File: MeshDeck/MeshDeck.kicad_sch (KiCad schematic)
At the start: 4 parts, among them CN1 ATGM336H-6N-74, U1 ESP32-S3-WROOM-1(N16R8), U2 SX1262S8S+T-X1, U3 TPS62827ADMQR

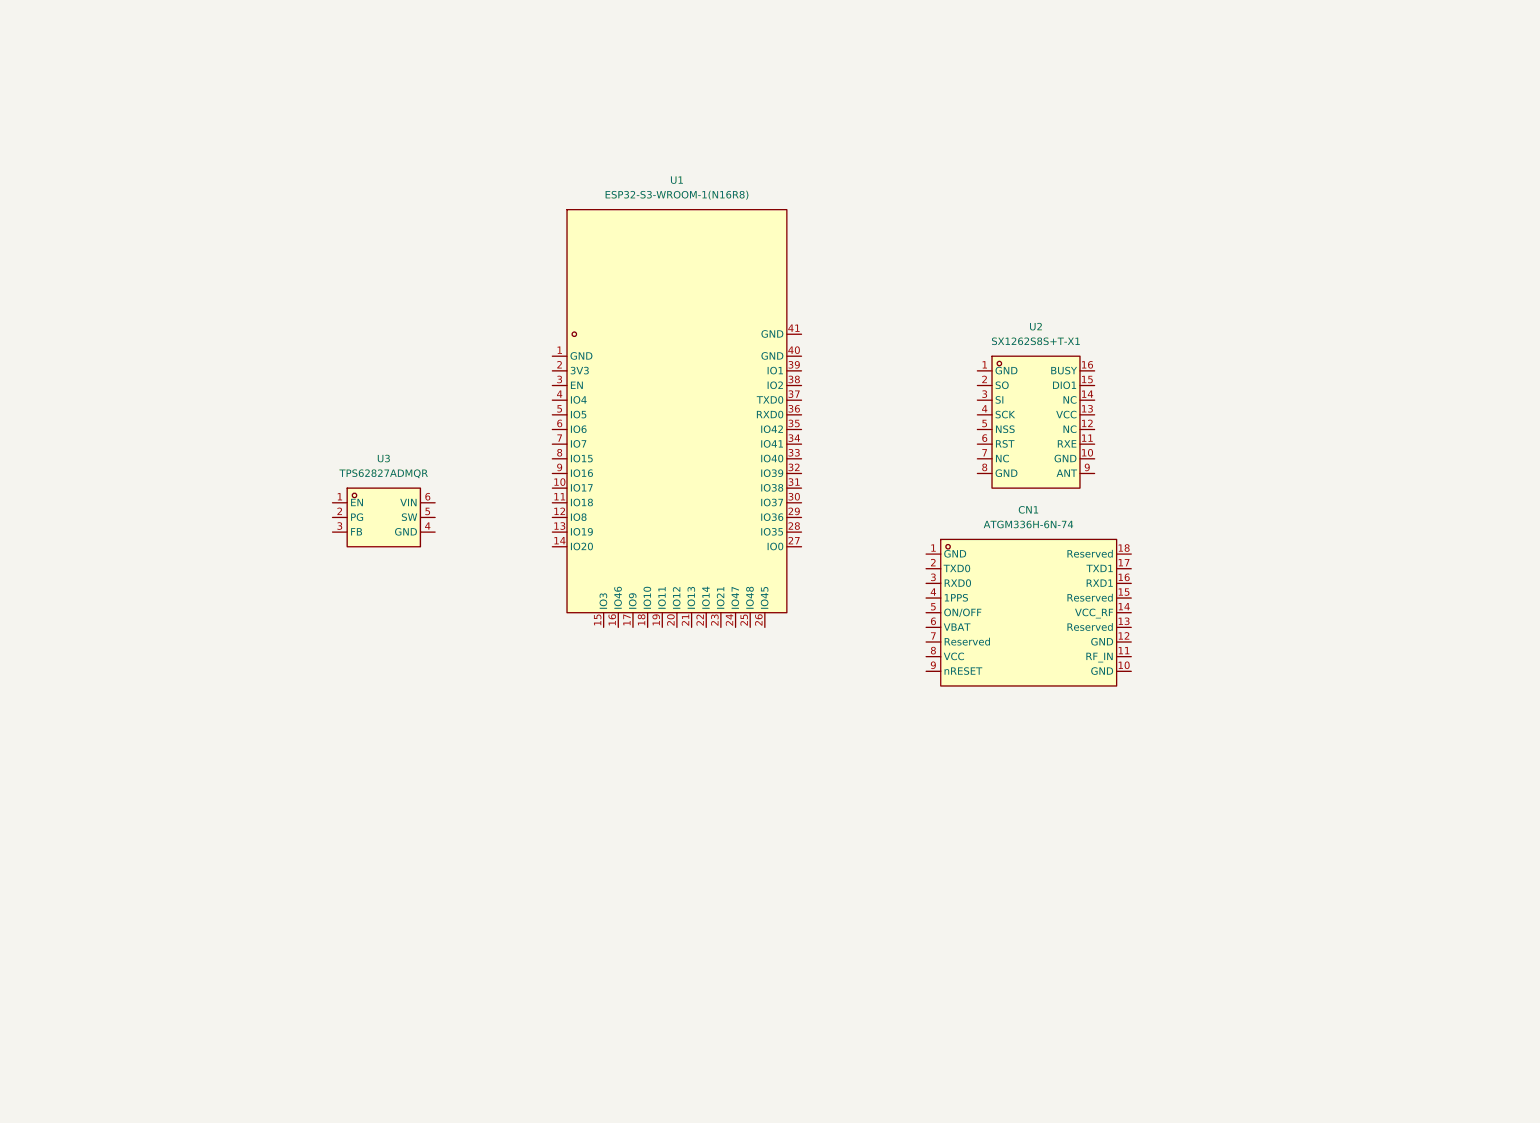
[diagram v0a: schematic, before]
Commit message: Added ESP-32 and USB stuff
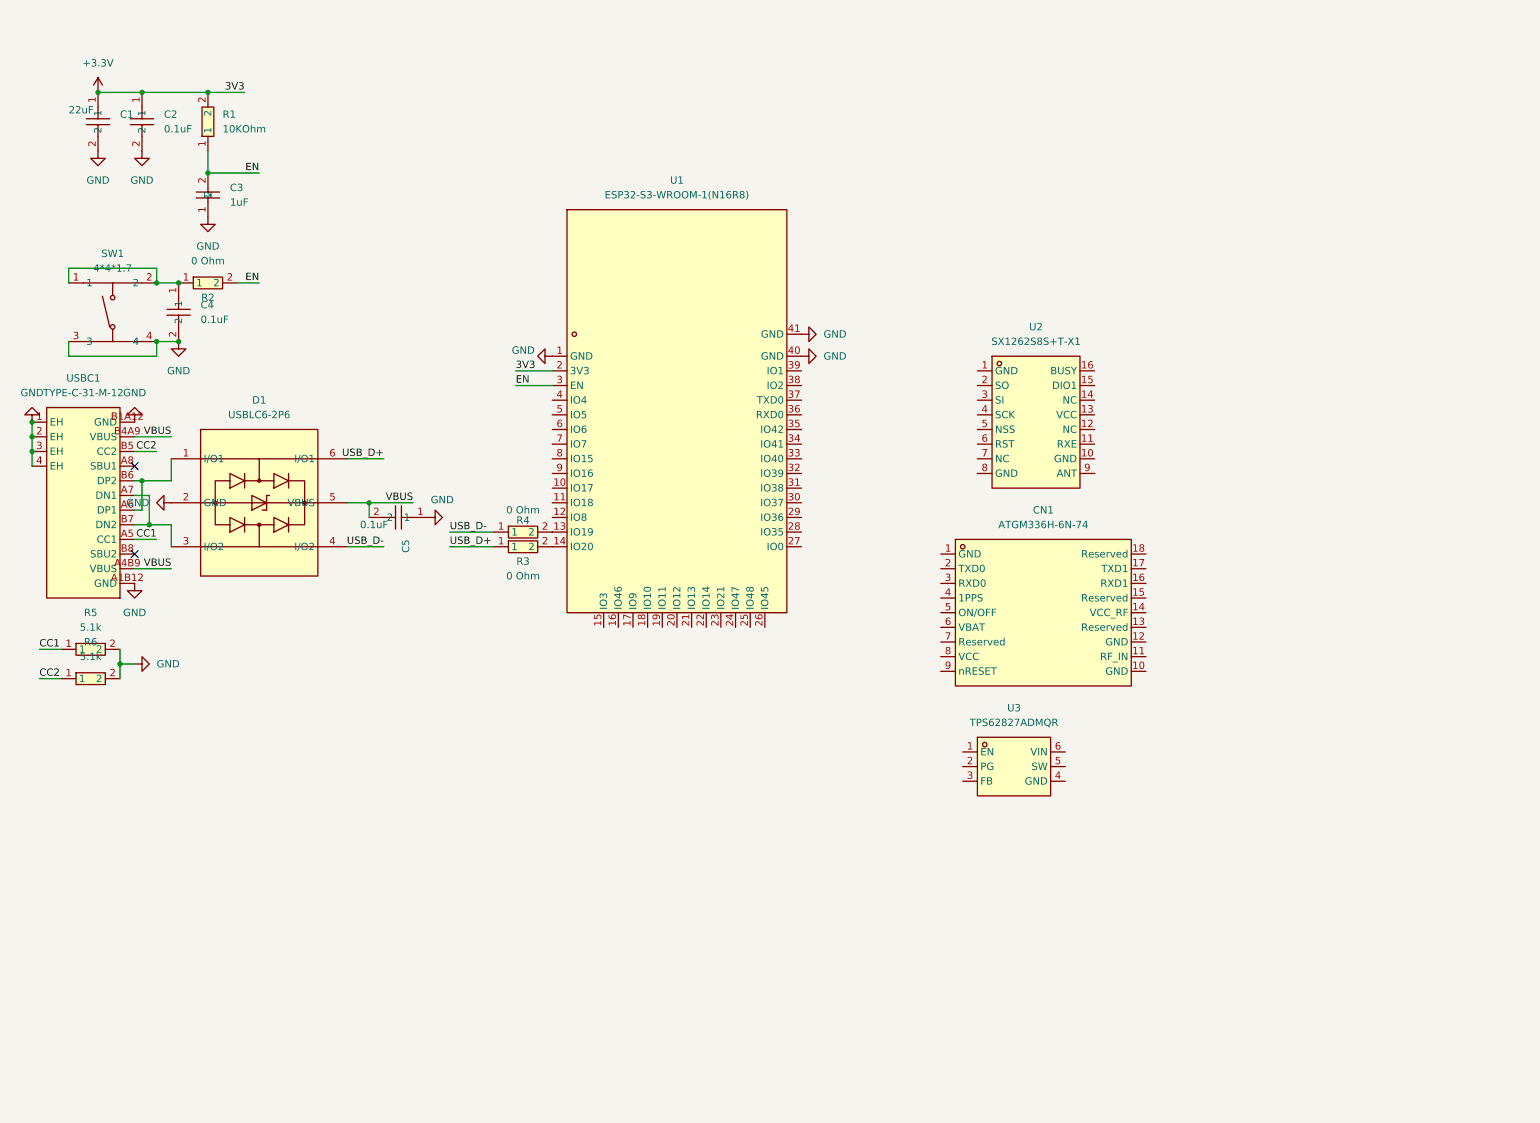
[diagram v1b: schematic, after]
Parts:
- added C1: 22uF, MeshDeck:C0402, symbol MeshDeck:CL05A226MQ5QUNC
- added C2, C4, C5: 0.1uF, MeshDeck:C0402, symbol MeshDeck:CL05B104KO5NNNC
- added C3: 1uF, MeshDeck:C0402, symbol MeshDeck:CL05A105KP5NNNC
- added D1: USBLC6-2P6, MeshDeck:SOT-666-6_L1.6-W1.2-P0.50-LS1.6-BR, symbol MeshDeck:USBLC6-2P6
- added R1: 10KOhm, MeshDeck:R0402, symbol MeshDeck:QR0402F1KQ10
- added R2, R3, R4: 0 Ohm, MeshDeck:R0402, symbol MeshDeck:0402WGF0000TCE
- added R5, R6: 5.1k, MeshDeck:R0402, symbol MeshDeck:0402WGF5101TCE
- added SW1: 4*4*1.7, MeshDeck:SW-SMD_4P-L5.2-W5.2-P3.70-LS6.5, symbol MeshDeck:4*4*1.7
- added USBC1: TYPE-C-31-M-12, MeshDeck:USB-C_SMD-TYPE-C-31-M-12_1, symbol MeshDeck:TYPE-C-31-M-12
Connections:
- net GND: now reaches U1.1 (GND)
- net GND: now also U1.40 (GND), U1.41 (GND), C1.2, C2.2, C3.1, C4.2, C5.1, D1.2 (GND), R5.2, R6.2, SW1.3, SW1.4, USBC1.1 (EH), USBC1.2 (EH), USBC1.3 (EH), USBC1.4 (EH), USBC1.A1B12 (GND), USBC1.B1A12 (GND)
- net at U1.13 (IO19): now also R4.2
- net at U1.14 (IO20): now also R3.2
- net +3.3V: now reaches U1.2 (3V3)
- net +3.3V: now also C1.1, C2.1, R1.2
- net EN: now reaches U1.3 (EN)
- net EN: now also C3.2, R1.1, R2.2
- new net: D1.1 (I/O1), USBC1.A6 (DP1), USBC1.B6 (DP2)
- new net: D1.3 (I/O2), USBC1.A7 (DN1), USBC1.B7 (DN2)
- new net: C4.1, R2.1, SW1.1, SW1.2
- new net CC1: R5.1, USBC1.A5 (CC1)
- new net CC2: R6.1, USBC1.B5 (CC2)
- new net USB_D+: D1.6 (I/O1), R3.1
- new net USB_D-: D1.4 (I/O2), R4.1
- new net VBUS: C5.2, D1.5 (VBUS), USBC1.A4B9 (VBUS), USBC1.B4A9 (VBUS)
- no-connect marks 0 -> 2
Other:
- moved on the sheet: CN1, U3

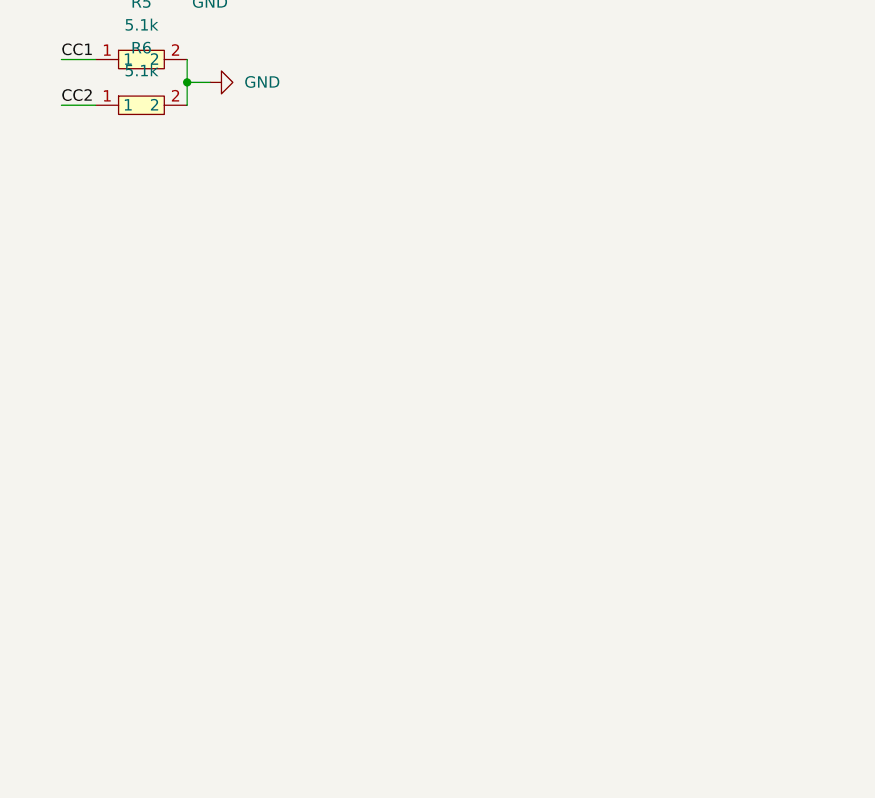
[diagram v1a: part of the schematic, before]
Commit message: added charging ic circuit
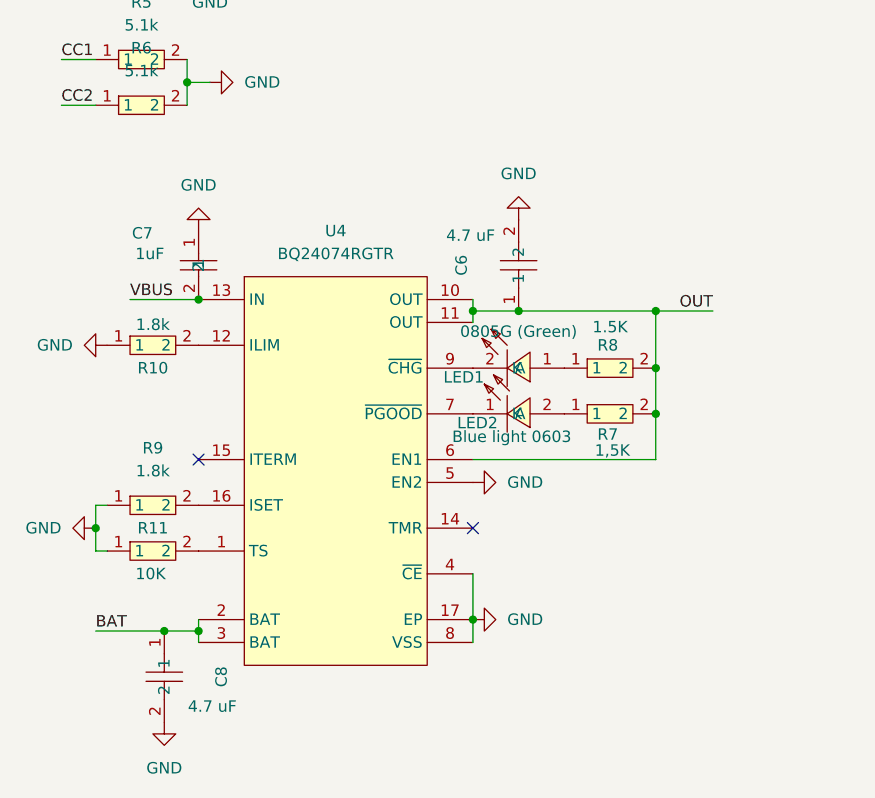
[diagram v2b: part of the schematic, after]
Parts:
- added C6, C8: 4.7 uF, MeshDeck:C0402, symbol MeshDeck:CL05A475MP5NRNC
- added C7: 1uF, MeshDeck:C0402, symbol MeshDeck:CL05A105KP5NNNC
- added LED1: 0805G (Green), MeshDeck:LED0805-R-RD, symbol MeshDeck:0805G(Green)
- added LED2: Blue light 0603, MeshDeck:LED0603-RD, symbol MeshDeck:Bluelight0603
- added R10, R9: 1.8k, MeshDeck:R0402, symbol MeshDeck:0402WGF1801TCE
- added R11: 10K, MeshDeck:R0402, symbol MeshDeck:0402WGF1002TCE
- added R7: 1,5K, MeshDeck:R0402, symbol MeshDeck:CR0402JF01R5G
- added R8: 1.5K, MeshDeck:R0402, symbol MeshDeck:CR0402JF01R5G
- added U4: BQ24074RGTR, MeshDeck:QFN-16_L3.0-W3.0-P0.50-TL-EP1.7, symbol MeshDeck:BQ24074RGTR
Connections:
- net GND: now also C6.2, C7.1, C8.2, R10.1, R11.1, R9.1, U4.17 (EP), U4.4 (~{CE}), U4.5 (EN2), U4.8 (VSS)
- net VBUS: now also C7.2, U4.13 (IN)
- new net: LED2.2 (A), R7.1
- new net: R11.2, U4.1 (TS)
- new net: R10.2, U4.12 (ILIM)
- new net: R9.2, U4.16 (ISET)
- new net: LED2.1 (K), U4.7 (~{PGOOD})
- new net: LED1.2 (K), U4.9 (~{CHG})
- new net: LED1.1 (A), R8.1
- new net BAT: C8.1, U4.2 (BAT), U4.3 (BAT)
- new net OUT: C6.1, R7.2, R8.2, U4.10 (OUT), U4.11 (OUT), U4.6 (EN1)
- no-connect marks 2 -> 4

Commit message: Added 3.3V step down converter
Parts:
- removed U3: TPS62827ADMQR, MeshDeck:VSON-6_L1.5-W1.5-P0.50-TL, symbol MeshDeck:TPS62827ADMQR
- added C10, C11, C12: 10uF, MeshDeck:C0402, symbol MeshDeck:CL05A106MQ5NUNC
- added C9: 4.7 uF, MeshDeck:C0402, symbol MeshDeck:CL05A475MP5NRNC
- added L1: 0.47 µH, MeshDeck:L0402, symbol MeshDeck:LSCNB1005EETR47MB
- added U3: TPS6282533DMQR, MeshDeck:VSON-6_L1.5-W1.5-P0.50-TL, symbol MeshDeck:TPS6282533DMQR
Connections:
- net OUT is gone; now on net +3.3V: C6.1, R7.2, R8.2, U4.10 (OUT), U4.11 (OUT), U4.6 (EN1)
- net +3.3V: now also C10.2, C11.2, C12.2, C9.1, U3.1 (EN), U3.3 (FB), U3.6 (VIN)
- net GND: now also C10.1, C11.1, C12.1, C9.2, U3.4 (GND)
- new net: L1.1, U3.5 (SW)
- no-connect marks 4 -> 5
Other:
- company: (none) -> ThePangel
- title: (none) -> MeshDeck
- moved on the sheet: CN1, R3, R4, U1, U2
